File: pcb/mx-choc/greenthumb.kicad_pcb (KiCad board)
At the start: 2 copper layers, 246.9 x 112.4 mm, 71 parts, among them J1 Conn_01x02_Female, M1 XIAO-RP2040, SW11 SW_Push, SW12 SW_Push, SW13 SW_Push, SW14 SW_Push, SW15 SW_Push, SW16 SW_Push, SW17 SW_Push, SW18 SW_Push, SW19 SW_Push, SW2 SW_Push, SW20 SW_Push, SW21 SW_Push, SW22 SW_Push, SW23 SW_Push, SW24 SW_Push, SW25 SW_Push, SW26 SW_Push, SW27 SW_Push, SW28 SW_Push, SW29 SW_Push, SW3 SW_Push, SW30 SW_Push, SW33 SW_Push, SW34 SW_Push, SW35 SW_Push, SW36 SW_Push, SW37 SW_Push, SW38 SW_Push, SW41 SW_Push, SW8 SW_Push, SW9 SW_Push

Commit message: routing almost done
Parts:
- moved ? 34.9 mm to (246.8, 30.0), turned to 15 degrees
- moved SW30 34.1 mm to (246.0, 41.5), turned to 30 degrees
- moved SW20 32.6 mm to (236.5, 25.1), turned to 30 degrees
- moved D30 32.1 mm to (238.6, 45.2), turned to -60 degrees
- moved D20 30.5 mm to (229.1, 28.8), turned to -60 degrees
- moved SW29 28.3 mm to (223.3, 40.2), turned to 30 degrees
- moved SW19 27.0 mm to (213.8, 23.7), turned to 30 degrees
- moved D21 26.9 mm to (21.7, 98.9), turned to -90 degrees
- moved SW9 26.6 mm to (204.3, 7.28), turned to 30 degrees
- moved D29 26.3 mm to (215.9, 43.9), turned to -60 degrees
- moved ? 25.6 mm to (23.2, 89.9), turned to 15 degrees
- moved D11 25.3 mm to (21.7, 79.9), turned to -90 degrees
- moved SW21 25.0 mm to (29.9, 99.4), turned to 0 degrees
- moved D19 24.9 mm to (206.4, 27.4), turned to -60 degrees
- moved D9 24.4 mm to (196.9, 11.0), turned to -60 degrees
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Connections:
- SW35 pad 2: unconnected-(SW35-Pad2) -> col0
- SW36 pad 2: unconnected-(SW36-Pad2) -> col0
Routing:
- net col2: track 3.48 -> 291.5 mm, vias 0 -> 6
- net col4: track 3.48 -> 216.6 mm, vias 0 -> 4
- net row0: track 3.62 -> 215.9 mm, vias 0 -> 7
- net col1: track 3.52 -> 198.4 mm, vias 0 -> 3
- net col5: track 3.44 -> 190.4 mm, vias 0 -> 4
- net row3: track 3.50 -> 189.1 mm, vias 0 -> 5
- net row4: track 3.36 -> 188.8 mm, vias 0 -> 5
- net col3: track 3.42 -> 185.3 mm, vias 0 -> 1
- net col0: track 3.56 -> 167.3 mm, vias 0 -> 3
- net row1: track 3.58 -> 82.6 mm, vias 0 -> 5
- net row2: track 3.54 -> 63.4 mm, vias 0 -> 3
- net Net-(D17-Pad2): track 0.00 -> 9.41 mm
- net Net-(D22-Pad2): track 0.00 -> 7.77 mm
- net Net-(D18-Pad2): track 0.00 -> 6.13 mm
- net Net-(D19-Pad2): track 0.00 -> 5.85 mm
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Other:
- board size 246.9 x 112.4 mm -> 238.7 x 135.7 mm

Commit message: completed pcb
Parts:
- added H1: MountingHole, fingerpunch:fingerpunch-logo, F.Cu at (149.6, 129.4)
- moved ? 44.3 mm to (264.5, 70.5), turned to 0 degrees
- moved SW20 42.7 mm to (255.9, 63.1), turned to 15 degrees
- moved SW30 42.6 mm to (260.8, 81.5), turned to 15 degrees
- moved D20 40.5 mm to (247.8, 64.8), turned to -75 degrees
- moved D30 40.4 mm to (252.7, 83.1), turned to -75 degrees
- moved SW9 39.3 mm to (229.4, 37.6), turned to 15 degrees
- moved SW19 38.2 mm to (234.3, 55.9), turned to 15 degrees
- moved SW29 37.6 mm to (239.2, 74.3), turned to 15 degrees
- moved D9 37.3 mm to (221.3, 39.2), turned to -75 degrees
- moved D19 36.1 mm to (226.2, 57.6), turned to -75 degrees
- moved ? 36.0 mm to (219.0, 45.0), turned to 0 degrees
- moved D29 35.5 mm to (231.1, 76.0), turned to -75 degrees
- moved SW8 35.1 mm to (209.7, 37.7), turned to 15 degrees
- moved SW18 33.6 mm to (214.6, 56.0), turned to 15 degrees
- moved D8 33.1 mm to (201.6, 39.3), turned to -75 degrees
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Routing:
- net col0: track 167.3 -> 357.8 mm, vias 3 -> 5
- net row2: track 63.4 -> 217.5 mm, vias 3 -> 9
- net row1: track 82.6 -> 224.5 mm, vias 5 -> 12
- net col3: track 185.3 -> 276.2 mm, vias 1 -> 6
- net col4: track 216.6 -> 306.5 mm, vias 4 -> 9
- net row0: track 215.9 -> 303.9 mm, vias 7 -> 12
- net col1: track 198.4 -> 275.7 mm, vias 3 -> 4
- net row3: track 189.1 -> 237.6 mm, vias 5 -> 6
- net GND: track 0.00 -> 36.6 mm, vias 0 -> 1
- net row4: track 188.8 -> 216.7 mm, vias 5 -> 6
- net RESET: track 0.00 -> 24.4 mm, vias 0 -> 1
- net Net-(D34-Pad2): track 0.00 -> 5.79 mm
- net Net-(D35-Pad2): track 0.00 -> 5.73 mm
- added copper zone on B.Cu, net GND
- added copper zone on F.Cu, net GND
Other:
- board size 238.7 x 135.7 mm -> 246.9 x 112.4 mm
- board text removed: "F"

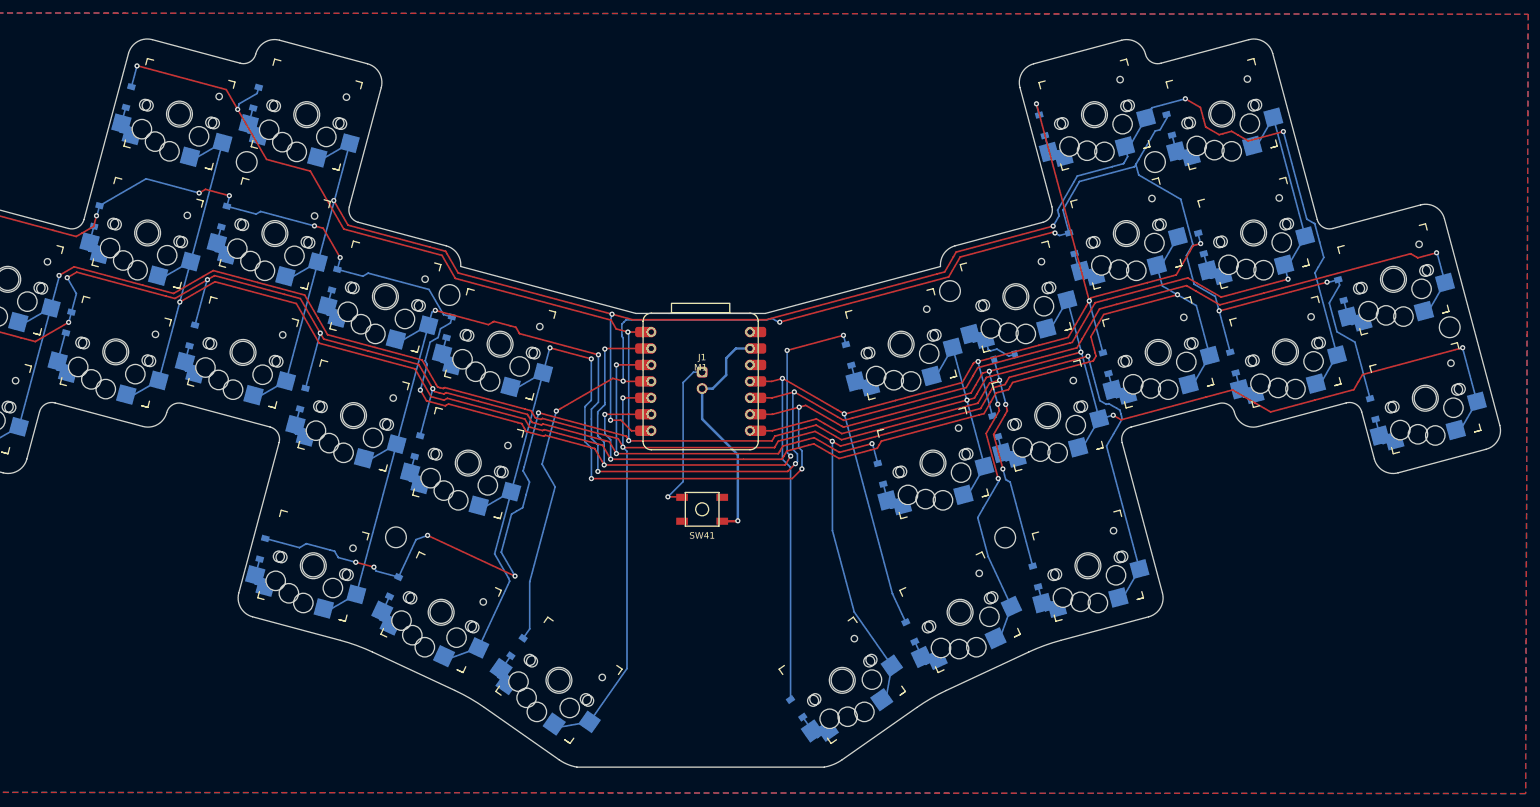
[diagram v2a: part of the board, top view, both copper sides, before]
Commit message: cleaned up some extra files, fixed fingerpunch logo orientation, moved reset switch to bottom of pcb
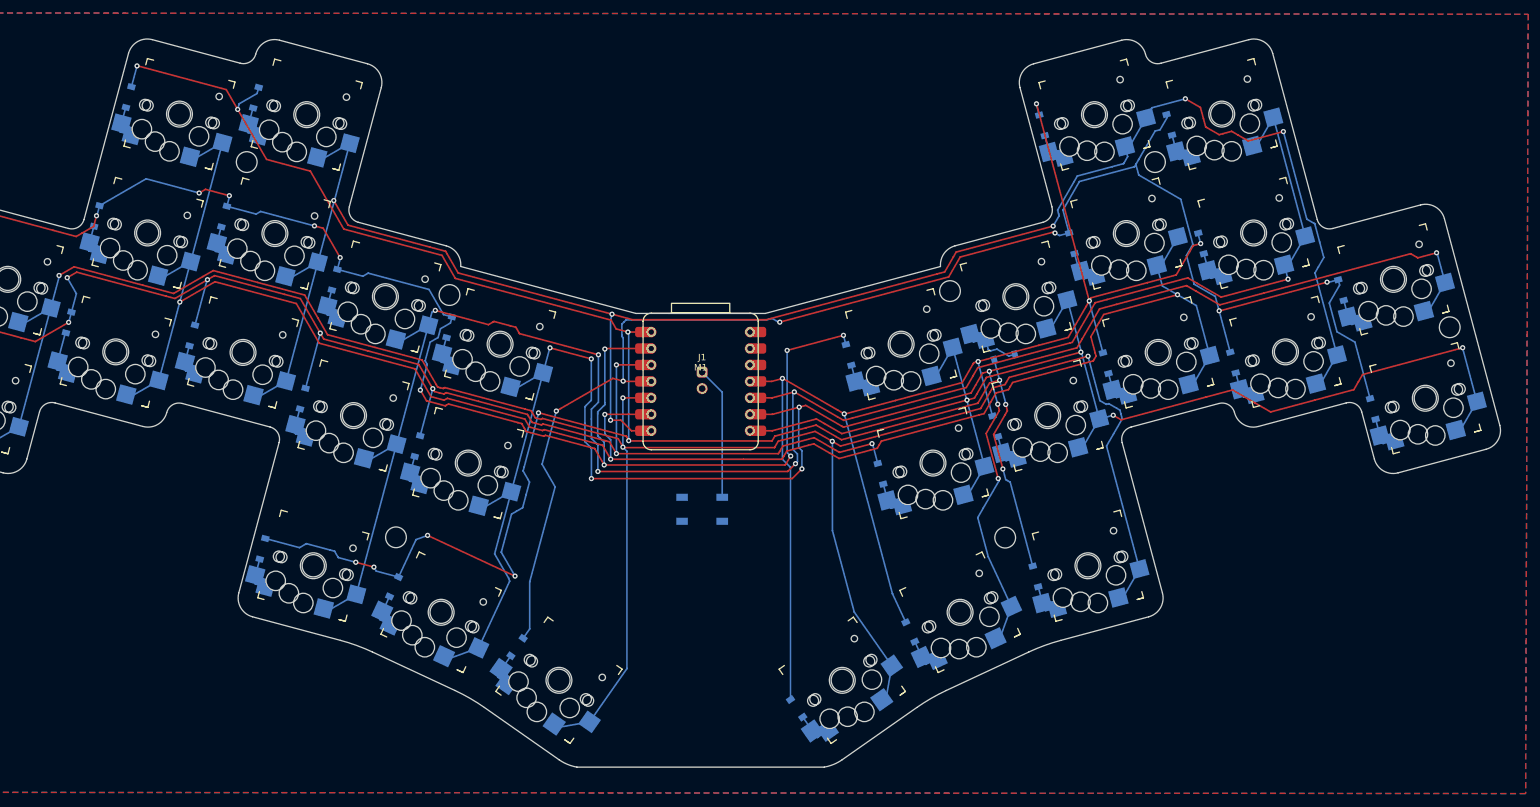
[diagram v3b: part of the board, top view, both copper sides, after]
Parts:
- H1, SW41: moved to B.Cu
- turned H1 to 180 degrees
- turned SW41 to 180 degrees
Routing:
- net GND: track 36.6 -> 0.00 mm, vias 1 -> 0
- net RESET: track 24.4 -> 20.6 mm, vias 1 -> 0

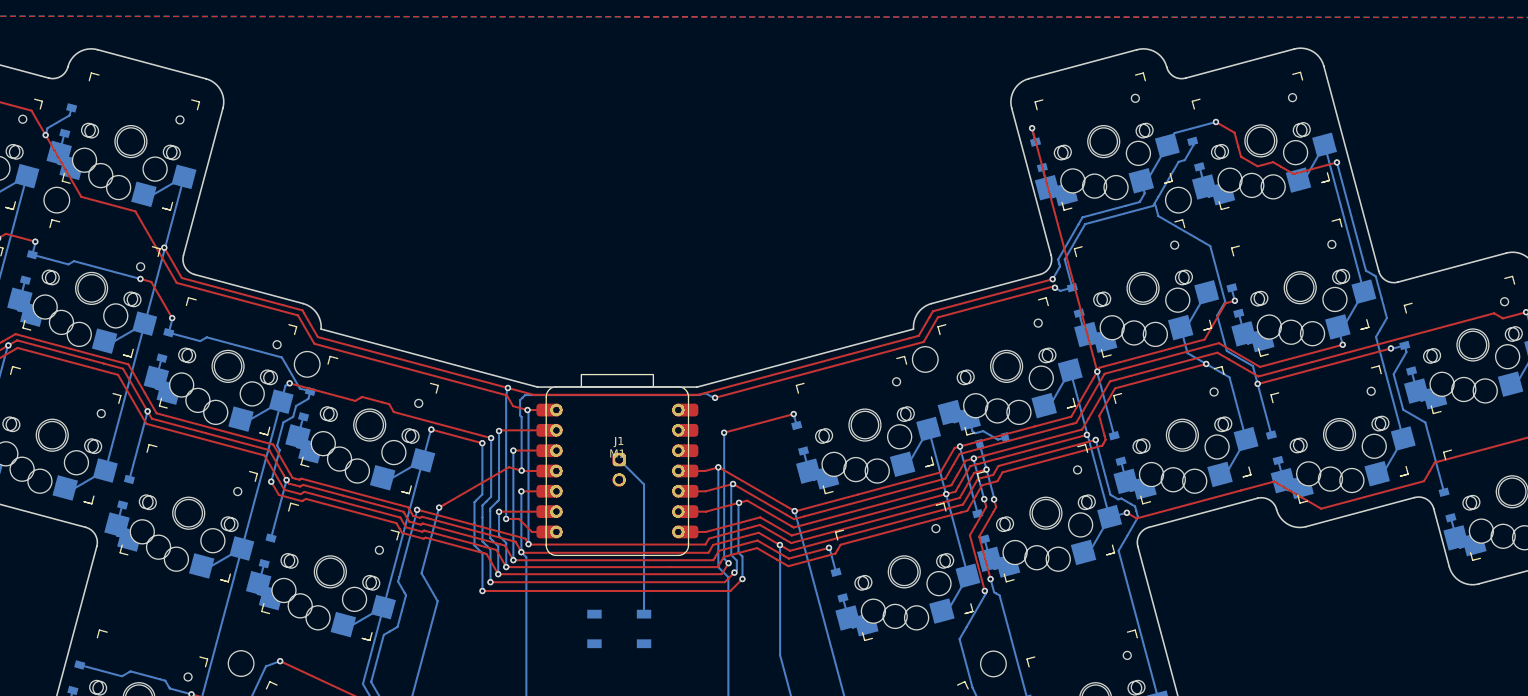
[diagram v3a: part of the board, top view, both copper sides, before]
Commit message: removed reset switch, as it wasn't being used, and no way to hook it up to the seeeduino
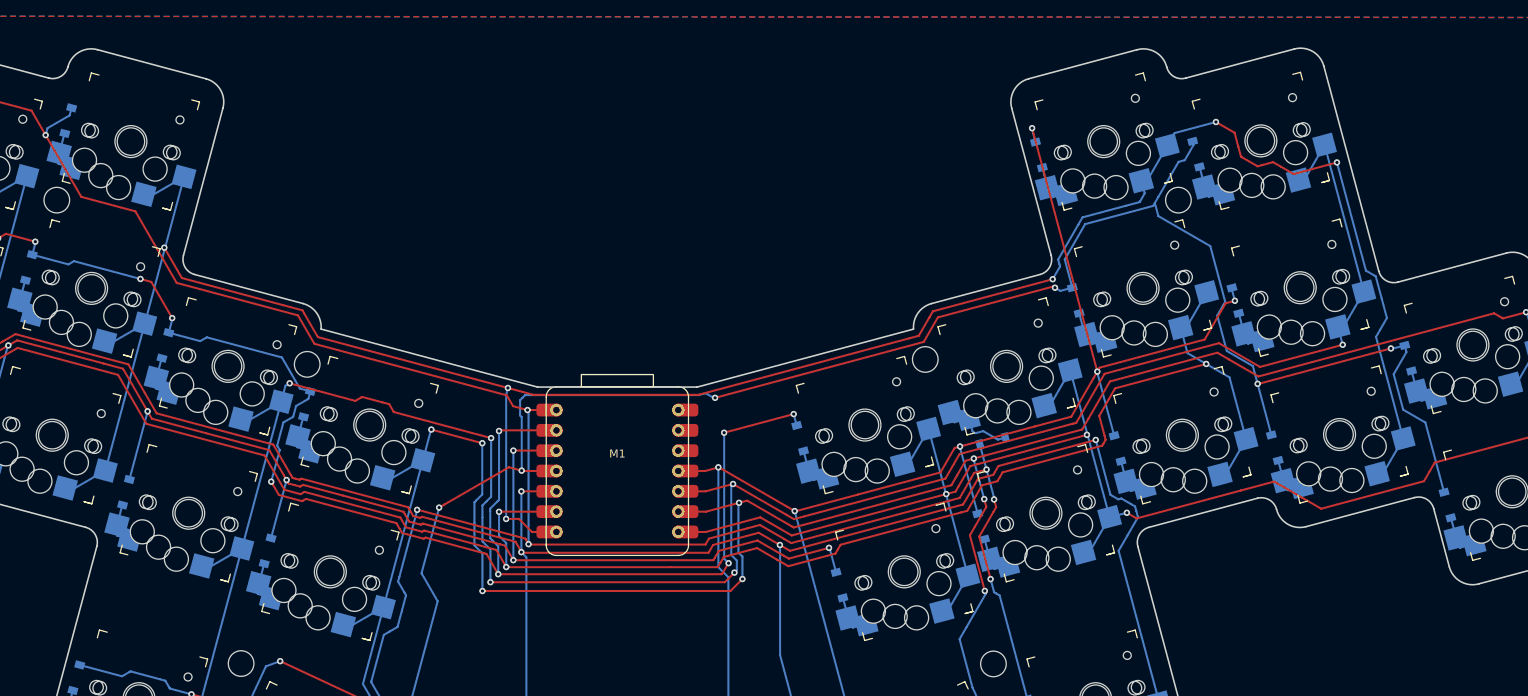
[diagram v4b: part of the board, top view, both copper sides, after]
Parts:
- removed J1: Conn_01x02_Female, fingerpunch:Connector_THT_1x2_2.54
- removed SW41: SW_Push, random-keyboard-parts:SKQG-1155865
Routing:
- net RESET: track 20.6 -> 0.00 mm
